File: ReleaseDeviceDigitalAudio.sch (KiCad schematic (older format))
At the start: 5 parts, among them J3 AudioJack3, J4 AudioJack3, J5 AudioJack3, J7 AudioJack3, J8 AudioJack3

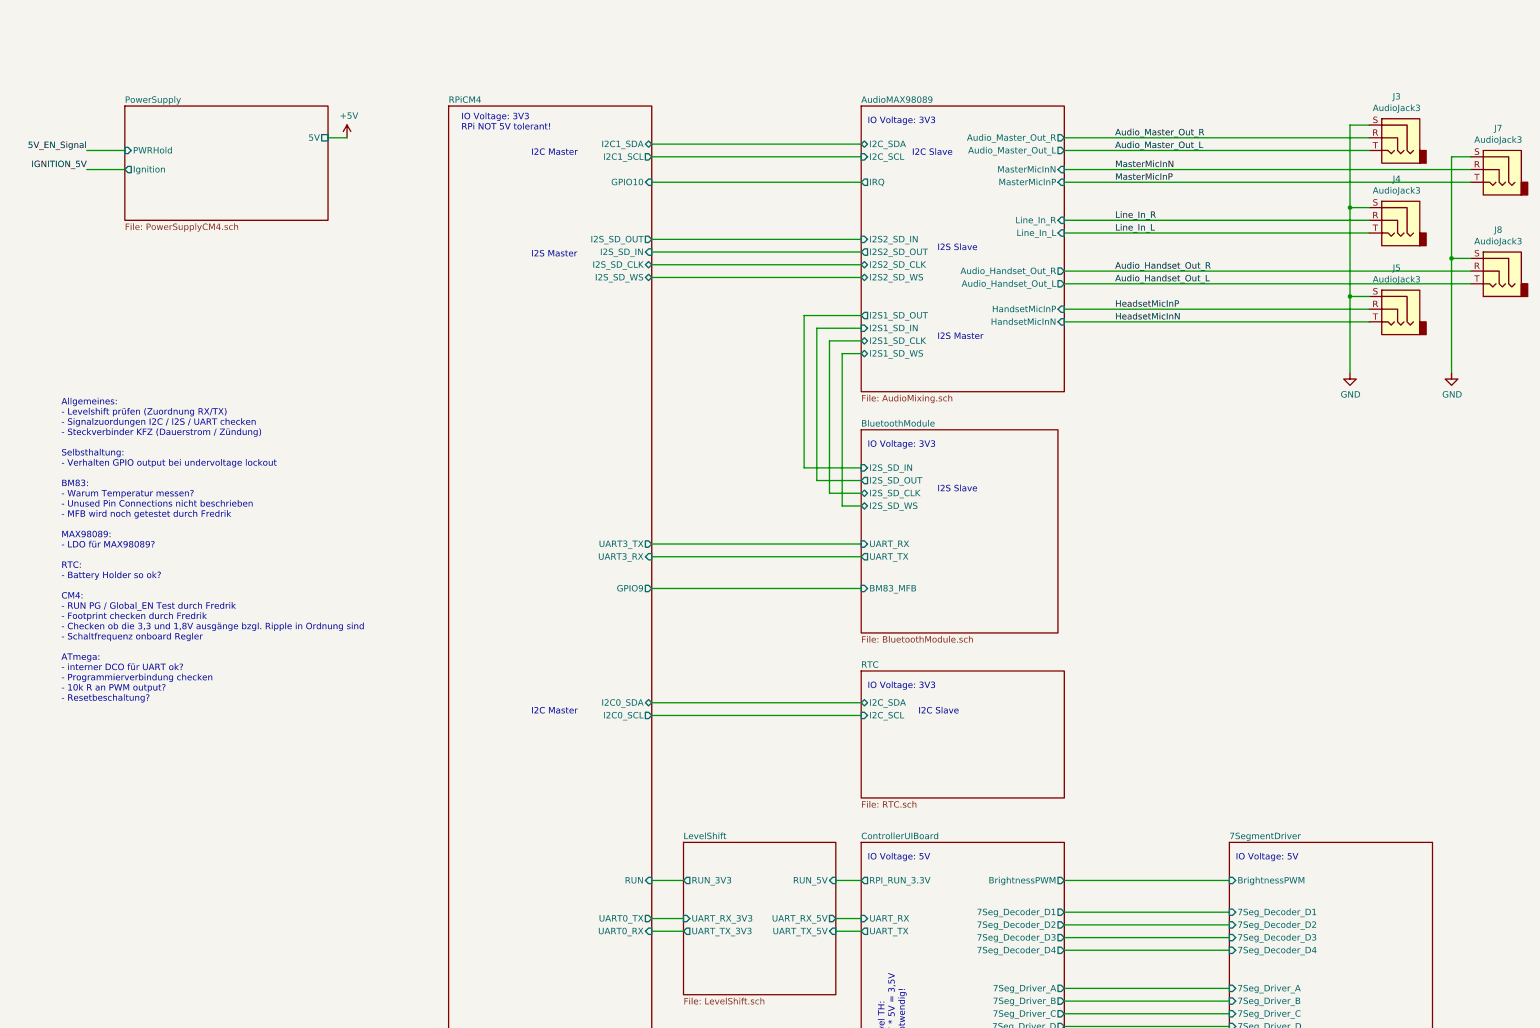
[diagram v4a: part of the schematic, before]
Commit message: - ATmega überarbeitet - Alle offenen Punkte zusammengefasst
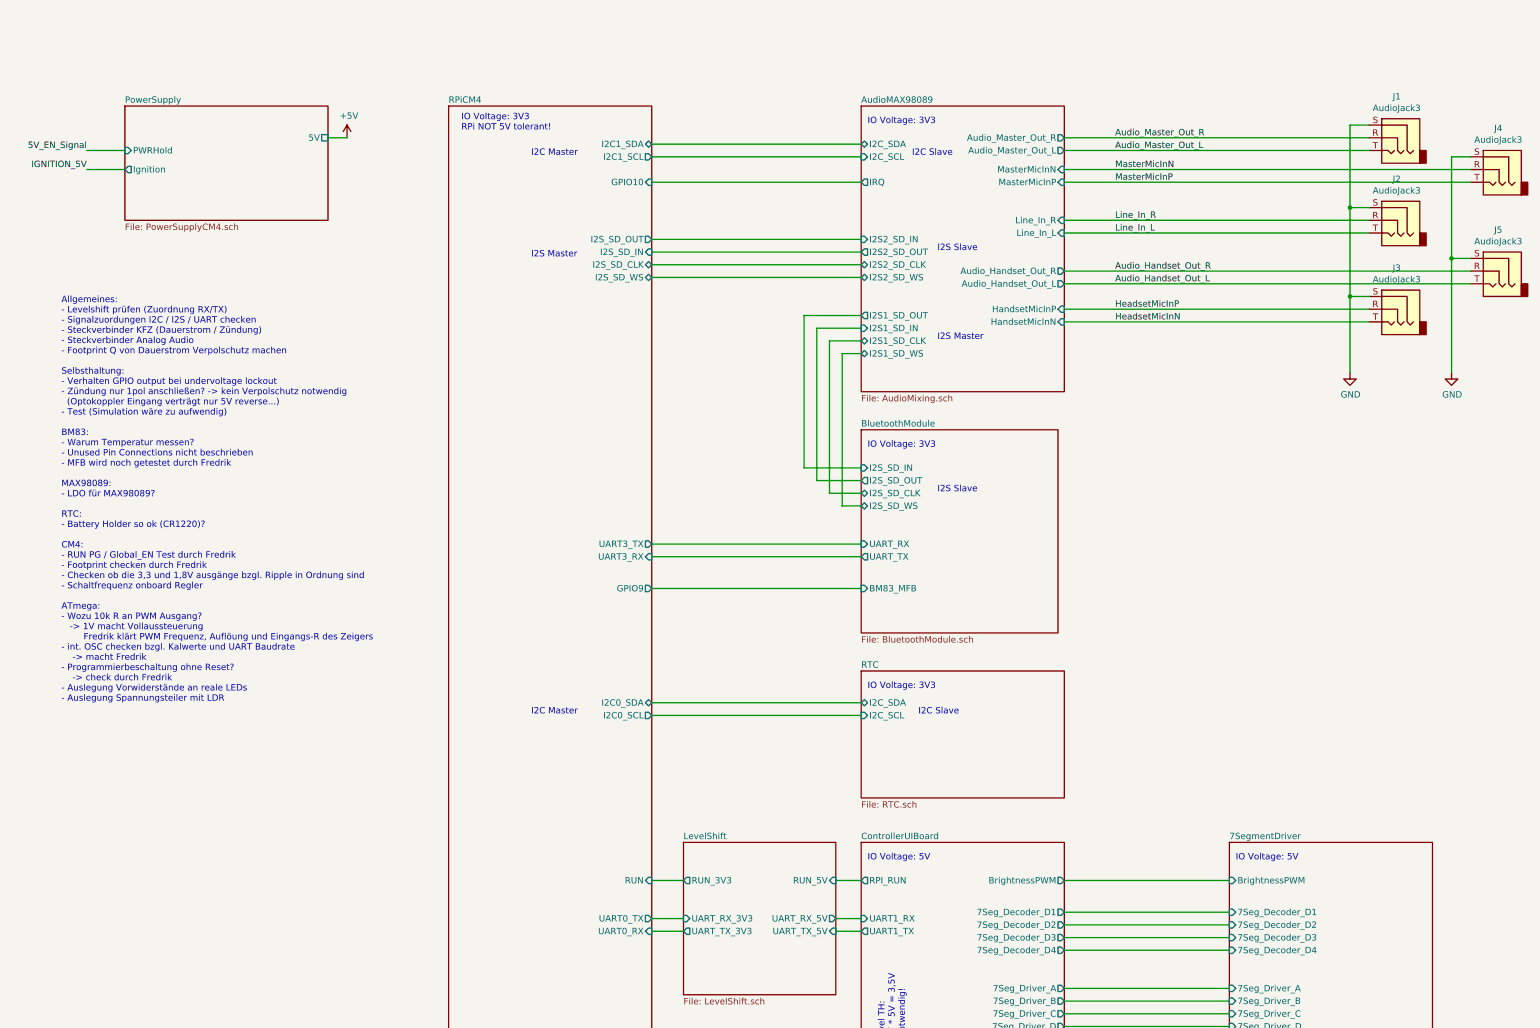
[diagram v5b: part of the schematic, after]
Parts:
- renumbered J3 to J1, J4 to J2, J5 to J3, J7 to J4, J8 to J5
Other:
- note added: "Allgemeines: \n- Levelshift prüfen (Zuordnung RX/TX)\n- Signalzuordungen I2C / I2S / UART checken\n- Steckverbinder KFZ (Dauerstrom / Zündung)\n- Steckverbinder Analog Audio\n- Footprint Q von Dauerstrom Verpolschutz machen\n\nSelbsthaltung:\n- Verhalten GPIO output bei undervoltage lockout\n- Zündung nur 1pol anschließen? -> kein Verpolschutz notwendig\n (Optokoppler Eingang verträgt nur 5V reve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"
- note removed: "Allgemeines: \n- Levelshift prüfen (Zuordnung RX/TX)\n- Signalzuordungen I2C / I2S / UART checken\n- Steckverbinder KFZ (Dauerstrom / Zündung)\n\nSelbsthaltung:\n- Verhalten GPIO output bei undervoltage lockout\n\nBM83:\n- Warum Temperatur messen?\n- Unused Pin Connections nicht beschrieben\n- MFB wird noch getestet durch Fredrik\n\nMAX98089:\n- LDO für MAX98089?\n\nRTC:\n- Battery Holder so ok?\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"
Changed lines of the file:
@@
 $EndDescr
 $Comp
-L Connector:AudioJack3 J7
+L Connector:AudioJack3 J4
 U 1 1 66962862
 P 12200 1850
-F 0 "J7" H 12182 2175 50  0000 C CNN
+F 0 "J4" H 12182 2175 50  0000 C CNN
 F 1 "AudioJack3" H 12182 2084 50  0000 C CNN
 F 2 "TeKaDe:LumbergKLB4" H 12200 1850 50  0001 C CNN
@@
 	3150 1600 3000 1600
 $Comp
-L Connector:AudioJack3 J3
+L Connector:AudioJack3 J1
 U 1 1 60575B8C
 P 11400 1600
-F 0 "J3" H 11382 1925 50  0000 C CNN
+F 0 "J1" H 11382 1925 50  0000 C CNN
 F 1 "AudioJack3" H 11382 1834 50  0000 C CNN
 F 2 "TeKaDe:LumbergKLB4" H 11400 1600 50  0001 C CNN
@@
 $EndComp
 $Comp
-L Connector:AudioJack3 J4
+L Connector:AudioJack3 J2
 U 1 1 6066C958
 P 11400 2250
-F 0 "J4" H 11382 2575 50  0000 C CNN
+F 0 "J2" H 11382 2575 50  0000 C CNN
 F 1 "AudioJack3" H 11382 2484 50  0000 C CNN
 F 2 "TeKaDe:LumbergKLB4" H 11400 2250 50  0001 C CNN
@@
 $EndComp
 $Comp
-L Connector:AudioJack3 J5
+L Connector:AudioJack3 J3
 U 1 1 6105818C
 P 11400 2950
-F 0 "J5" H 11382 3275 50  0000 C CNN
+F 0 "J3" H 11382 3275 50  0000 C CNN
 F 1 "AudioJack3" H 11382 3184 50  0000 C CNN
 F 2 "TeKaDe:LumbergKLB4" H 11400 2950 50  0001 C CNN
@@
 $EndComp
 $Comp
-L Connector:AudioJack3 J8
+L Connector:AudioJack3 J5
 U 1 1 6123782D
 P 12200 2650
-F 0 "J8" H 12182 2975 50  0000 C CNN
+F 0 "J5" H 12182 2975 50  0000 C CNN
 F 1 "AudioJack3" H 12182 2884 50  0000 C CNN
 F 2 "TeKaDe:LumbergKLB4" H 12200 2650 50  0001 C CNN
@@
 Wire Wire Line
 	11850 2550 11850 3450
-$Sheet
-S 7200 7150 1600 2550
-U 60F18E7A
-F0 "ControllerUIBoard" 50
-F1 "ControllerUIBoard.sch" 50
-F2 "RPI_RUN_3.3V" O L 7200 7450 50
-F3 "IGNITION_SENSE" I R 8800 9150 50
-F4 "5V_EN_OUT" O R 8800 9300 50
-F5 "UART_RX" I L 7200 7750 50
-F6 "UART_TX" O L 7200 7850 50
-F7 "7Seg_Driver_D" O R 8800 8600 50
-F8 "7Seg_Driver_C" O R 8800 8500 50
-F9 "7Seg_Driver_B" O R 8800 8400 50
-F10 "7Seg_Driver_A" O R 8800 8300 50
-F11 "7Seg_Decoder_D3" O R 8800 7900 50
-F12 "7Seg_Decoder_D4" O R 8800 8000 50
-F13 "7Seg_Decoder_D2" O R 8800 7800 50
-F14 "7Seg_Decoder_D1" O R 8800 7700 50
-F15 "BrightnessPWM" O R 8800 7450 50
-$EndSheet
 Text Label 9100 9150 0    50   ~ 0
 IGNITION_5V
@@
 	8800 2650 12000 2650
 Text Notes 900  6050 0    50   ~ 0
-Allgemeines: \n- Levelshift prüfen (Zuordnung RX/TX)\n- Signalzuordungen I2C / I2S / UART checken\n- Steckverbinder KFZ (Dauerstrom / Zündung)\n\nSelbsthaltung:\n- Verhalten GPIO output bei undervoltage lockout\n\nBM83:\n- Warum Temperatur messen?\n- Unused Pin Connections nicht beschrieben\n- MFB wird noch getestet durch Fredrik\n\nMAX98089:\n- LDO für MAX98089?\n\nRTC:\n- Battery Holder so ok?\n\nCM4: \n- RUN PG / Global_EN Test durch Fredrik\n- Footprint checken durch Fredrik\n- Checken ob die 3,3 und 1,8V ausgänge bzgl. Ripple in Ordnung sind\n- Schaltfrequenz onboard Regler\n\nATmega:\n- interner DCO für UART ok?\n- Programmierverbindung checken\n- 10k R an PWM output?\n- Resetbeschaltung?\n
+Allgemeines: \n- Levelshift prüfen (Zuordnung RX/TX)\n- Signalzuordungen I2C / I2S / UART checken\n- Steckverbinder KFZ (Dauerstrom / Zündung)\n- Steckverbinder Analog Audio\n- Footprint Q von Dauerstrom Verpolschutz machen\n\nSelbsthaltung:\n- Verhalten GPIO output bei undervoltage lockout\n- Zündung nur 1pol anschließen? -> kein Verpolschutz notwendig\n  (Optokoppler Eingang verträgt nur 5V reverse...)\n- Test (Simulation wäre zu aufwendig)\n\nBM83:\n- Warum Temperatur messen?\n- Unused Pin Connections nicht beschrieben\n- MFB wird noch getestet durch Fredrik\n\nMAX98089:\n- LDO für MAX98089?\n\nRTC:\n- Battery Holder so ok (CR1220)?\n\nCM4: \n- RUN PG / Global_EN Test durch Fredrik\n- Footprint checken durch Fredrik\n- Checken ob die 3,3 und 1,8V ausgänge bzgl. Ripple in Ordnung sind\n- Schaltfrequenz onboard Regler\n\nATmega:\n- Wozu 10k R an PWM Ausgang?\n   -> 1V macht Vollaussteuerung\n        Fredrik klärt PWM Frequenz, Auflöung und Eingangs-R des Zeigers\n- int. OSC checken bzgl. Kalwerte und UART Baudrate\n    -> macht Fredrik\n- Programmierbeschaltung ohne Reset?\n    -> check durch Fredrik\n- Auslegung Vorwiderstände an reale LEDs\n- Auslegung Spannungsteiler mit LDR\n
 $Comp
 L power:GND #PWR02
@@
 F4 "Ignition" O L 1400 1850 50
 $EndSheet
+$Sheet
+S 7200 7150 1600 2550
+U 60F18E7A
+F0 "ControllerUIBoard" 50
+F1 "ControllerUIBoard.sch" 50
+F2 "IGNITION_SENSE" I R 8800 9150 50
+F3 "5V_EN_OUT" O R 8800 9300 50
+F4 "7Seg_Driver_D" O R 8800 8600 50
+F5 "7Seg_Driver_C" O R 8800 8500 50
+F6 "7Seg_Driver_B" O R 8800 8400 50
+F7 "7Seg_Driver_A" O R 8800 8300 50
+F8 "7Seg_Decoder_D3" O R 8800 7900 50
+F9 "7Seg_Decoder_D4" O R 8800 8000 50
+F10 "7Seg_Decoder_D2" O R 8800 7800 50
+F11 "7Seg_Decoder_D1" O R 8800 7700 50
+F12 "BrightnessPWM" O R 8800 7450 50
+F13 "RPI_RUN" O L 7200 7450 50
+F14 "UART1_RX" I L 7200 7750 50
+F15 "UART1_TX" O L 7200 7850 50
+$EndSheet
 $EndSCHEMATC

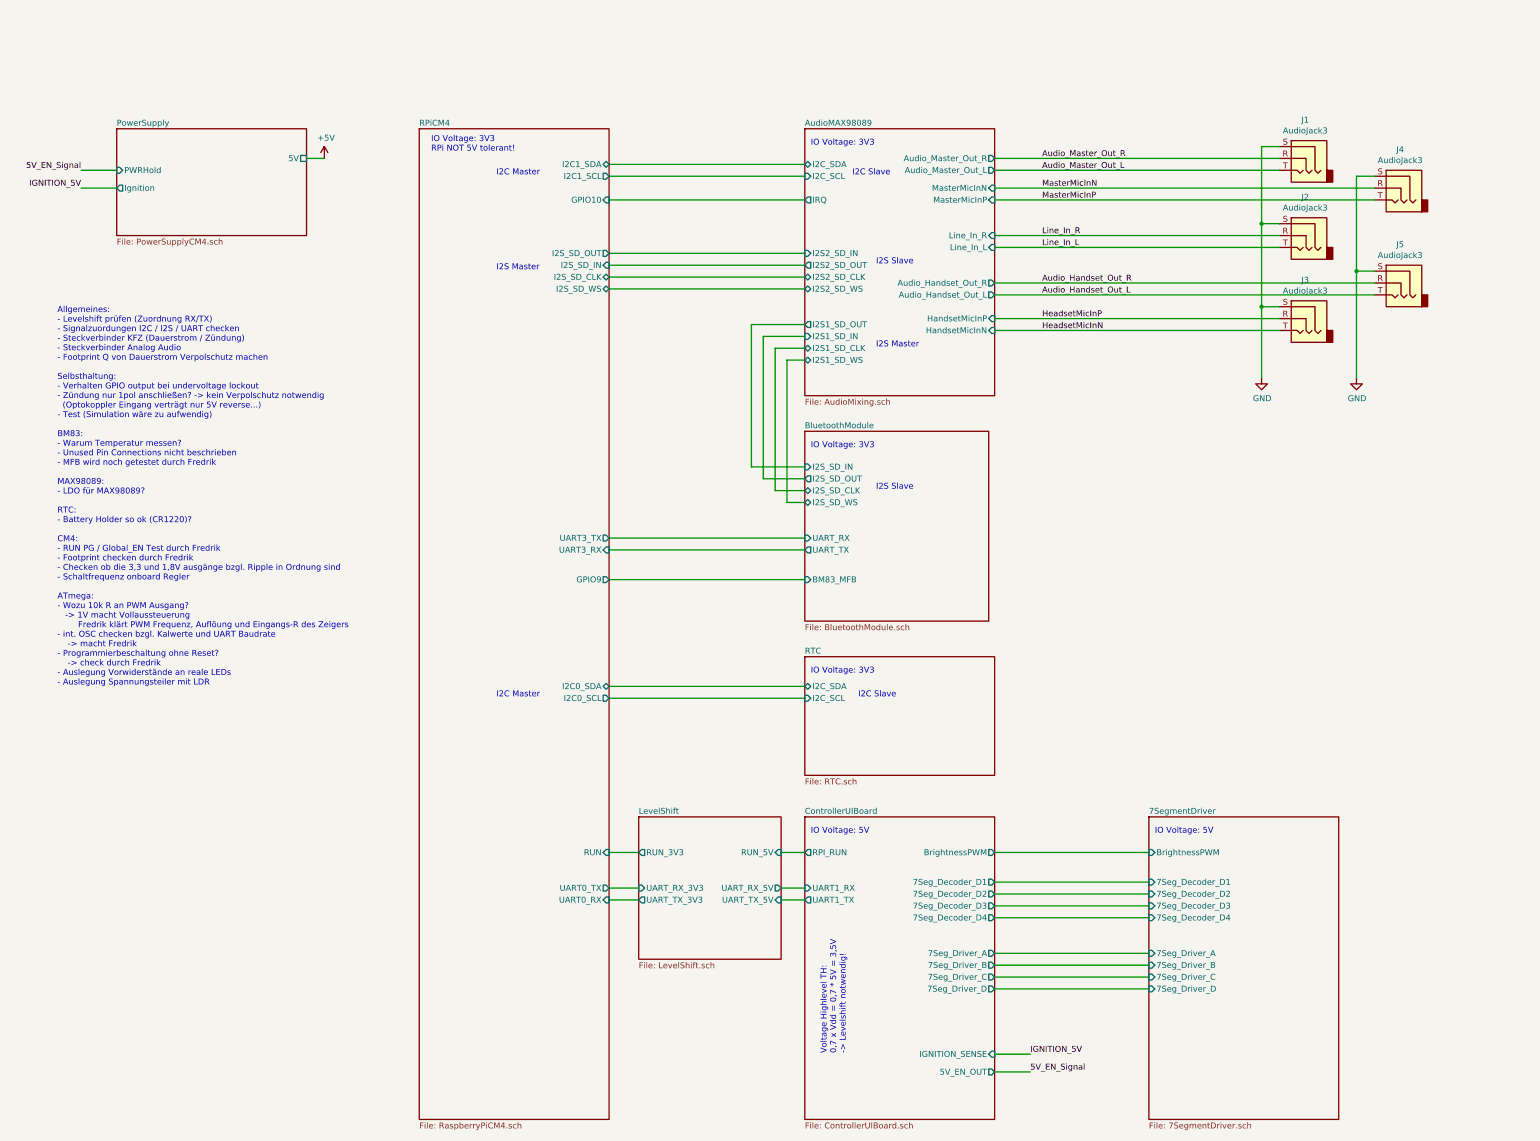
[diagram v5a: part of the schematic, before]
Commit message: - Platzoptimierungen
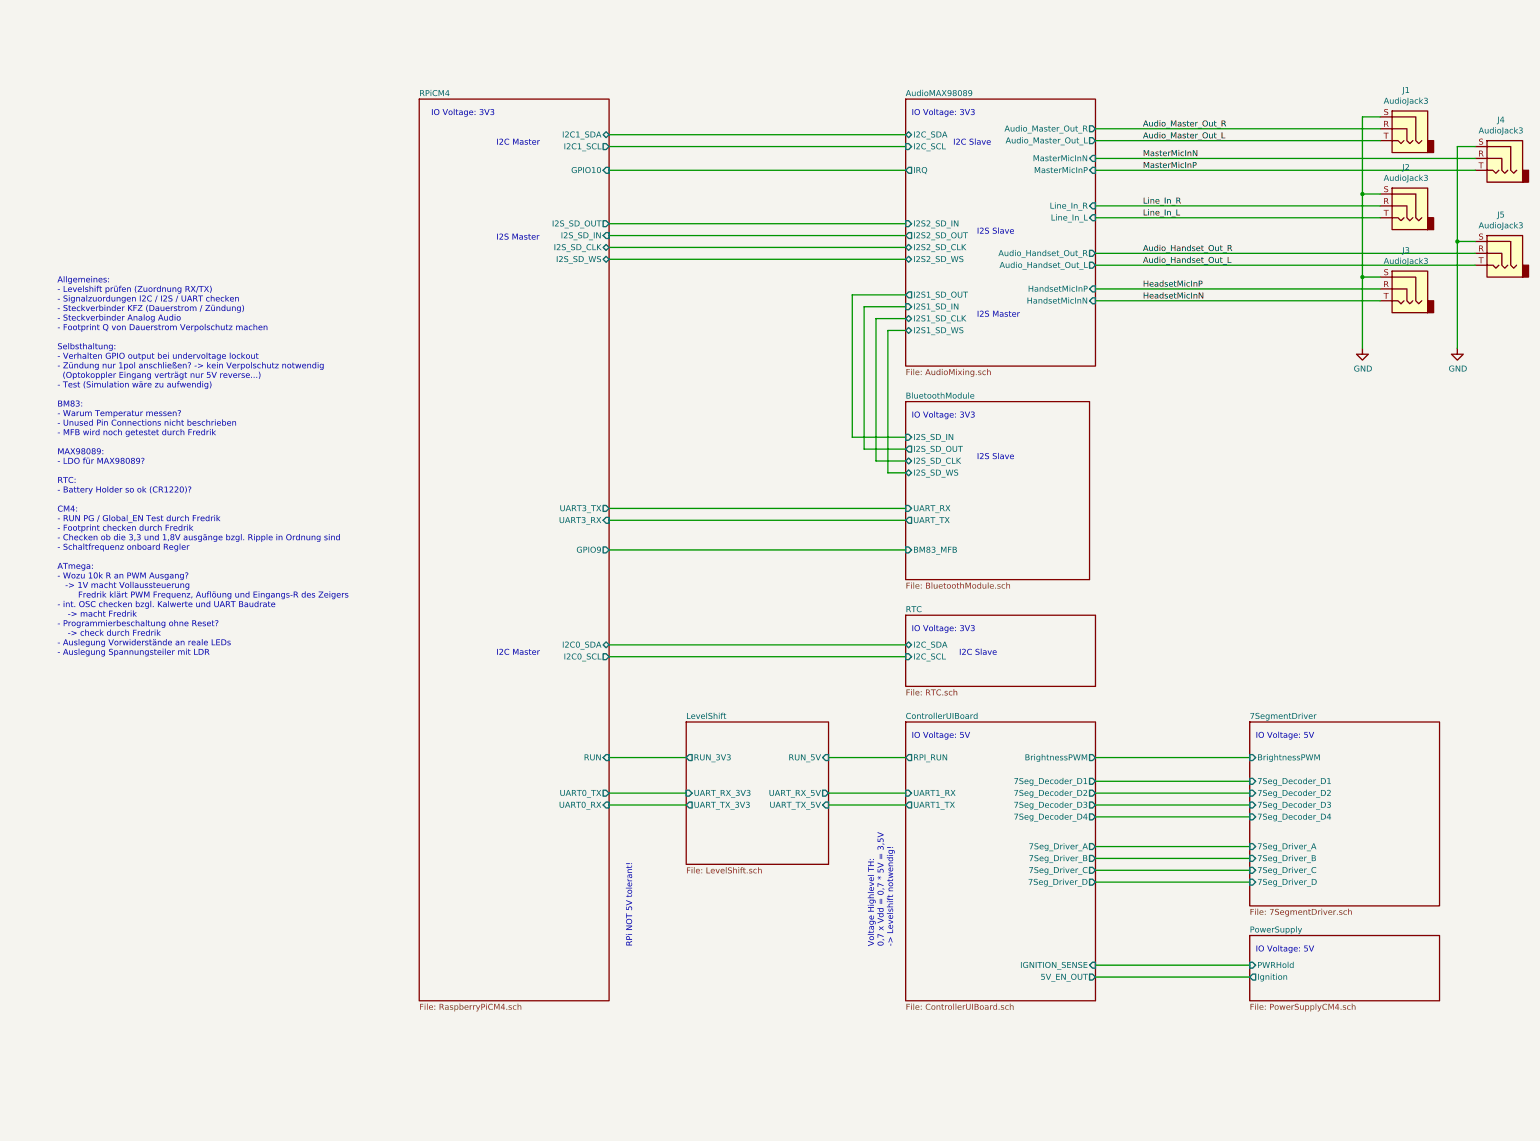
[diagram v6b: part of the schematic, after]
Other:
- note added: "IO Voltage: 3V3\n"
- note added: "RPi NOT 5V tolerant!"
- note removed: "IO Voltage: 3V3\nRPi NOT 5V tolerant!\n"
- moved on the sheet: J1, J2, J3, J4, J5
